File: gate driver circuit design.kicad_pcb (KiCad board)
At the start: 2 copper layers, 40 x 40 mm, 105 parts, among them J101 90122-0763, J102 90121-0762, J103 90121-0762, Q1 CSD17313Q2, Q2 MMBT3904T-7-F, Q3 MMBT3904T-7-F, Q4 MMBT3904T-7-F, T1 750343725, T2 750343725, U1 SN6501QDBVRQ1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

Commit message: Almost Done Routing Of PCB
Some Connections are remaining , Almost Done Routing Of PCB
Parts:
- moved R12 35.9 mm to (115.9, 57.9)
- moved R14 34.6 mm to (115.8, 50.5), turned to -90 degrees
- moved U8 32.5 mm to (81.2, 60.8), turned to -90 degrees
- moved C39 30.7 mm to (111.4, 58.0), turned to 90 degrees
- moved C18 30.1 mm to (110.6, 65.0)
- moved C40 29.4 mm to (110.6, 50.5), turned to 90 degrees
- moved U7 29.3 mm to (83.1, 73.5), turned to 90 degrees
- moved U2 27.0 mm to (81.6, 52.7)
- moved C35 25.6 mm to (80.3, 81.3)
- moved C19 24.9 mm to (108.0, 64.9)
- moved R132 24.5 mm to (107.3, 85.1)
- moved R7 24.5 mm to (108.0, 57.5), turned to -90 degrees
- moved R33 24.4 mm to (107.3, 80.9)
- moved R28 24.1 mm to (86.2, 55.6)
- moved R23 23.6 mm to (82.1, 83.4), turned to 0 degrees
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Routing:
- net -4Vb: track 0.00 -> 90.0 mm, vias 0 -> 11
- net 5Vin: track 0.00 -> 65.4 mm, vias 0 -> 8
- net Comb: track 0.00 -> 62.5 mm, vias 0 -> 4
- net RESET: track 0.00 -> 49.5 mm, vias 0 -> 2
- net GND: track 0.00 -> 49.5 mm, vias 0 -> 7
- net Coma: track 0.00 -> 49.0 mm, vias 0 -> 3
- net -4Va: track 0.00 -> 47.2 mm, vias 0 -> 1
- net Vcc5V: track 0.00 -> 45.4 mm, vias 0 -> 9
- net +15Vb: track 0.00 -> 44.4 mm, vias 0 -> 2
- net Net-(D3-K): track 0.00 -> 38.8 mm
- net +15Va: track 0.00 -> 38.2 mm, vias 0 -> 6
- net FLT: track 0.00 -> 33.7 mm, vias 0 -> 2
- net G2: track 0.00 -> 33.0 mm, vias 0 -> 2
- net Net-(D4-K): track 0.00 -> 24.1 mm, vias 0 -> 2
- net Net-(U7-OUTB): track 0.00 -> 22.9 mm, vias 0 -> 1
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- added copper zone on B.Cu, net (none)
- added copper zone on F.Cu, net (none)
- added copper zone on B.Cu, net -4Vb
- added copper zone on F.Cu, net -4Vb
- added copper zone on B.Cu, net GND
- added copper zone on F.Cu, net GND
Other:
- outline, holes or cut-outs redrawn

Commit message: routing
routing
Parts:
- moved C20 3.88 mm to (106.4, 68.7)
- moved C19 3.88 mm to (108.8, 68.7)
- moved C18 3.76 mm to (111.8, 68.6)
- moved Q2 3.28 mm to (83.0, 63.3)
- moved C15 2.79 mm to (87.5, 53.5)
- moved R9 2.72 mm to (98.2, 82.5), turned to 180 degrees
- moved C35 2.66 mm to (80.5, 78.7), turned to 0 degrees
- moved T1 1.98 mm to (105.0, 73.6)
- moved C31 1.98 mm to (97.7, 64.9)
- moved C8 1.76 mm to (110.0, 55.4)
- moved C29 1.76 mm to (96.0, 64.9)
- moved C33 1.69 mm to (81.5, 65.9)
- moved D6 1.68 mm to (101.3, 50.4), turned to 180 degrees
- moved C14 1.59 mm to (88.2, 58.0), turned to 90 degrees
- moved C28 1.54 mm to (93.5, 65.1)
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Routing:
- net -4Vb: track 90.0 -> 0.00 mm, vias 11 -> 0
- net Comb: track 62.5 -> 0.00 mm, vias 4 -> 0
- net Coma: track 49.0 -> 0.00 mm, vias 3 -> 0
- net -4Va: track 47.2 -> 0.00 mm, vias 1 -> 0
- net Vcc5V: track 45.4 -> 0.00 mm, vias 9 -> 0
- net +15Vb: track 44.4 -> 0.00 mm, vias 2 -> 0
- net Net-(D3-K): track 38.8 -> 0.00 mm
- net +15Va: track 38.2 -> 0.00 mm, vias 6 -> 0
- net GND: track 49.5 -> 15.4 mm, vias 7 -> 2
- net G2: track 33.0 -> 0.00 mm, vias 2 -> 0
- net Net-(D4-K): track 24.1 -> 0.00 mm, vias 2 -> 0
- net Net-(U7-OUTB): track 22.9 -> 0.00 mm, vias 1 -> 0
- net Net-(Q3-C): track 22.2 -> 0.00 mm, vias 4 -> 0
- net Net-(U8--IN_A): track 21.2 -> 0.00 mm, vias 3 -> 0
- net Net-(C25-Pad1): track 17.2 -> 0.00 mm
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- removed copper zone on B.Cu, net (none)
- removed copper zone on F.Cu, net (none)
- removed copper zone on B.Cu, net -4Vb
- removed copper zone on F.Cu, net -4Vb
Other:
- outline, holes or cut-outs redrawn

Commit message: PCB Routing Last Stage
PCB Routing Last Stage
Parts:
- R132, R31, R33, R34: footprint ERJ-U060R00V:ERJS06_U06__0805_ -> CR0805-FX-5101ELF:RESC2012X60N
- R9: moved to F.Cu
- moved U5 54.7 mm to (39.9, 59.0)
- moved R6 53.9 mm to (37.0, 58.8)
- moved R5 50.4 mm to (44.0, 55.5)
- moved C27 50.3 mm to (48.7, 69.9)
- moved C30 49.9 mm to (46.9, 69.9)
- moved C26 49.5 mm to (44.4, 69.7)
- moved R10 49.3 mm to (52.2, 56.3)
- moved C24 48.9 mm to (50.2, 55.5)
- moved D5 48.6 mm to (50.2, 51.7)
- moved R15 48.5 mm to (52.0, 52.2)
- moved R11 48.5 mm to (48.1, 56.3), turned to 90 degrees
- moved R132 48.0 mm to (59.2, 84.1), turned to -90 degrees
- moved D4 48.0 mm to (50.9, 60.6)
- moved C25 48.0 mm to (46.0, 55.5)
- moved R9 47.9 mm to (50.3, 82.3), turned to 0 degrees
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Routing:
- net Comb: track 0.00 -> 71.0 mm, vias 0 -> 4
- net -4Vb: track 0.00 -> 60.1 mm, vias 0 -> 6
- net -4Va: track 0.00 -> 48.2 mm, vias 0 -> 3
- net Vcc5V: track 0.00 -> 39.0 mm, vias 0 -> 5
- net +15Vb: track 0.00 -> 33.6 mm, vias 0 -> 2
- net +15Va: track 0.00 -> 32.0 mm, vias 0 -> 1
- net Net-(U7-OUTB): track 0.00 -> 29.3 mm, vias 0 -> 1
- net Net-(D4-K): track 0.00 -> 26.2 mm
- net Net-(U8--IN_A): track 0.00 -> 18.7 mm
- net Coma: track 0.00 -> 18.7 mm, vias 0 -> 3
- net Net-(D3-K): track 0.00 -> 17.9 mm
- net Net-(J101-Pad4): track 4.59 -> 18.5 mm, vias 0 -> 2
- net Net-(Q3-C): track 0.00 -> 13.0 mm, vias 0 -> 1
- net Net-(D7-A): track 0.00 -> 11.7 mm, vias 0 -> 2
- net Net-(D5-A): track 0.00 -> 11.1 mm, vias 0 -> 1
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- added copper zone on B.Cu, net -4Vb
- added copper zone on F.Cu, net -4Vb
- added copper zone on F.Cu, net Coma
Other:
- board size 40 x 40 mm -> 40 x 40.3 mm

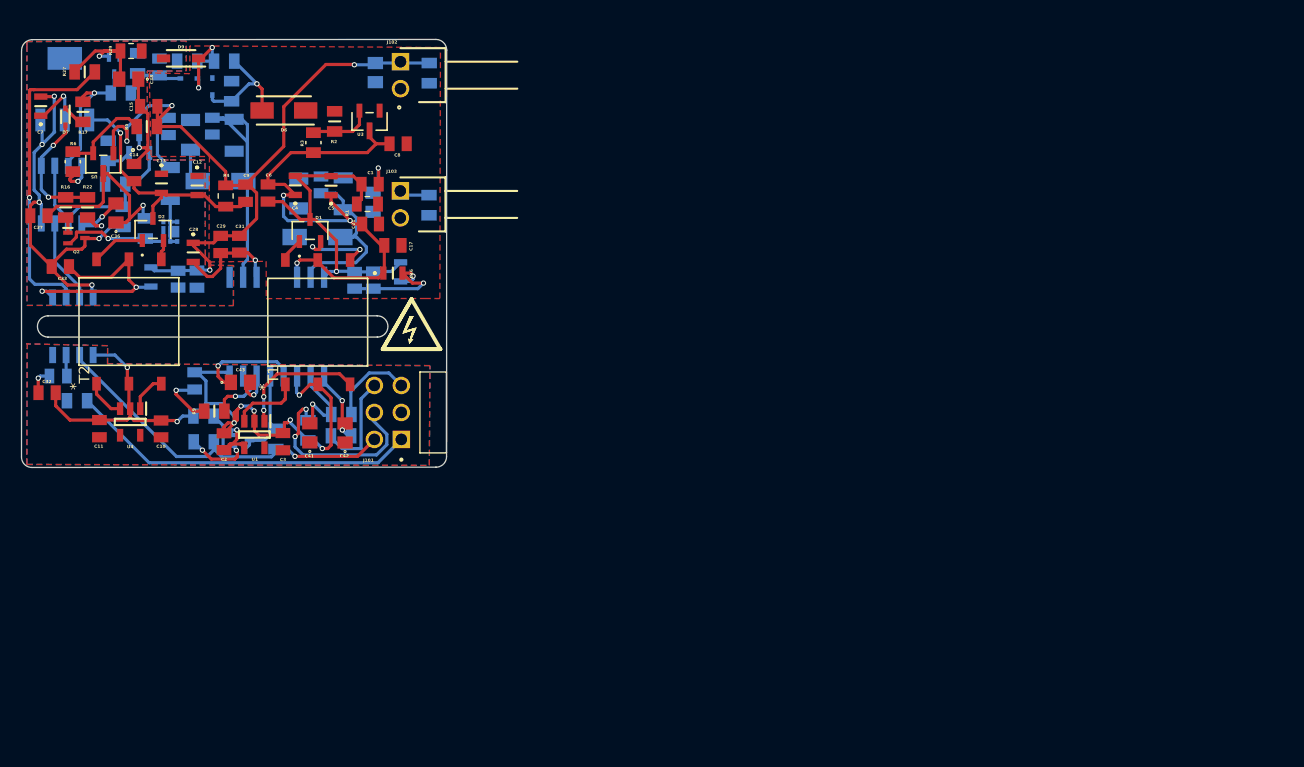
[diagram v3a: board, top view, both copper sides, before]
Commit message: Final PCB design TI gate driver
TI gate driver final PCB design files
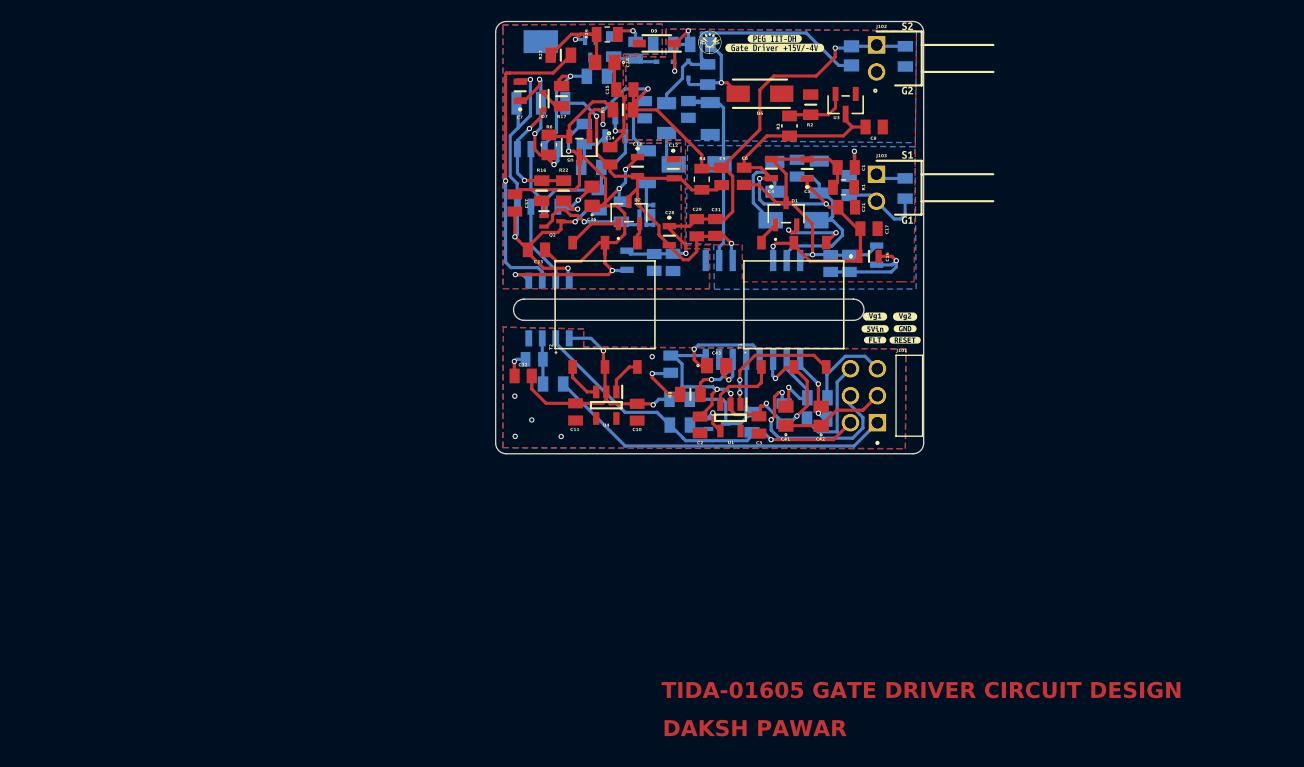
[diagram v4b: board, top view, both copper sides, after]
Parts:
- added G***: LOGO, PEG_LOGO:PEG_LOGO, F.Cu at (97.0, 47.6)
- added kibuzzard-666C5967: G***, kibuzzard-666C5967, F.Cu at (115.6, 46.0)
- added kibuzzard-666C5988: G***, kibuzzard-666C5988, F.Cu at (115.6, 58.2)
- added kibuzzard-666C5994: G***, kibuzzard-666C5994, F.Cu at (115.6, 64.3)
- added kibuzzard-666C5A2D: G***, kibuzzard-666C5A2D, F.Cu at (115.4, 73.4)
- added kibuzzard-666C5A33: G***, kibuzzard-666C5A33, F.Cu at (112.6, 73.4)
- added kibuzzard-666C5A3A: G***, kibuzzard-666C5A3A, F.Cu at (112.6, 74.5)
- added kibuzzard-666C5A3F: G***, kibuzzard-666C5A3F, F.Cu at (112.6, 75.6)
- added kibuzzard-666C5A43: G***, kibuzzard-666C5A43, F.Cu at (115.4, 74.5)
- added kibuzzard-666C5A49: G***, kibuzzard-666C5A49, F.Cu at (115.4, 75.6)
- added kibuzzard-666C5B08: G***, kibuzzard-666C5B08, F.Cu at (103.1, 47.2)
- added kibuzzard-666C5B11: G***, kibuzzard-666C5B11, F.Cu at (103.1, 48.1)
- added kibuzzard-666C5DC5: G***, kibuzzard-666C5DC5, B.Cu at (103.5, 48.1)
- added kibuzzard-666C5DEE: G***, kibuzzard-666C5DEE, B.Cu at (103.5, 47.2)
- added kibuzzard-666C5E10: G***, kibuzzard-666C5E10, F.Cu at (115.6, 52.1)
- moved C7 45.2 mm to (79.1, 52.2)
- moved D7 45.1 mm to (81.4, 53.1)
- moved R17 45.1 mm to (83.0, 52.6)
- moved R29 44.9 mm to (87.3, 46.8)
- moved T1 44.9 mm to (104.9, 72.3)
- moved C10 44.9 mm to (90.2, 82.4)
- moved C18 44.9 mm to (112.7, 67.6)
- moved C27 44.9 mm to (93.5, 68.3)
- moved C29 44.9 mm to (95.8, 65.0)
- moved C31 44.9 mm to (97.5, 65.0)
- moved C32 44.9 mm to (79.4, 79.0)
- moved C36 44.9 mm to (85.9, 62.1)
- moved C38 44.9 mm to (87.1, 49.5)
- moved C40 44.9 mm to (110.3, 48.8)
- moved C43 44.9 mm to (97.6, 78.0)
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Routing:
- net -4Vb: track 60.1 -> 86.8 mm, vias 6 -> 10
- net G2: track 0.00 -> 25.3 mm
- net Net-(D3-A): track 0.00 -> 8.32 mm
- net G1: track 0.00 -> 7.87 mm
- net GND: track 23.6 -> 30.4 mm, vias 4 -> 9
- net +15Vb: track 33.6 -> 40.3 mm
- net 5Vin: track 66.6 -> 60.5 mm, vias 8 -> 7
- net Net-(Q4-B): track 6.10 -> 2.15 mm, vias 2 -> 0
- net Net-(D4-K): track 26.2 -> 23.0 mm
- net Net-(U7-INB): track 2.01 -> 4.33 mm
- net FLT: track 35.4 -> 33.5 mm
- net Net-(D5-A): track 11.1 -> 9.72 mm
- net Comb: track 71.0 -> 72.0 mm
- net Coma: track 18.7 -> 17.8 mm, vias 3 -> 2
- net Vcc5V: track 39.0 -> 38.5 mm, vias 5 -> 4
- added copper zone on B.Cu, net G1
- added copper zone on B.Cu, net G2
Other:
- board size 40 x 40.3 mm -> 40.3 x 40.7 mm
- board text added: "DAKSH PAWAR"
- board text added: "TIDA-01605 GATE DRIVER CIRCUIT DESIGN"
